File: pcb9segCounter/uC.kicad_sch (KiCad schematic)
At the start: 15 parts, among them J1 SAO, J2 AVR-ISP-6, U1 ATtiny84A-SS

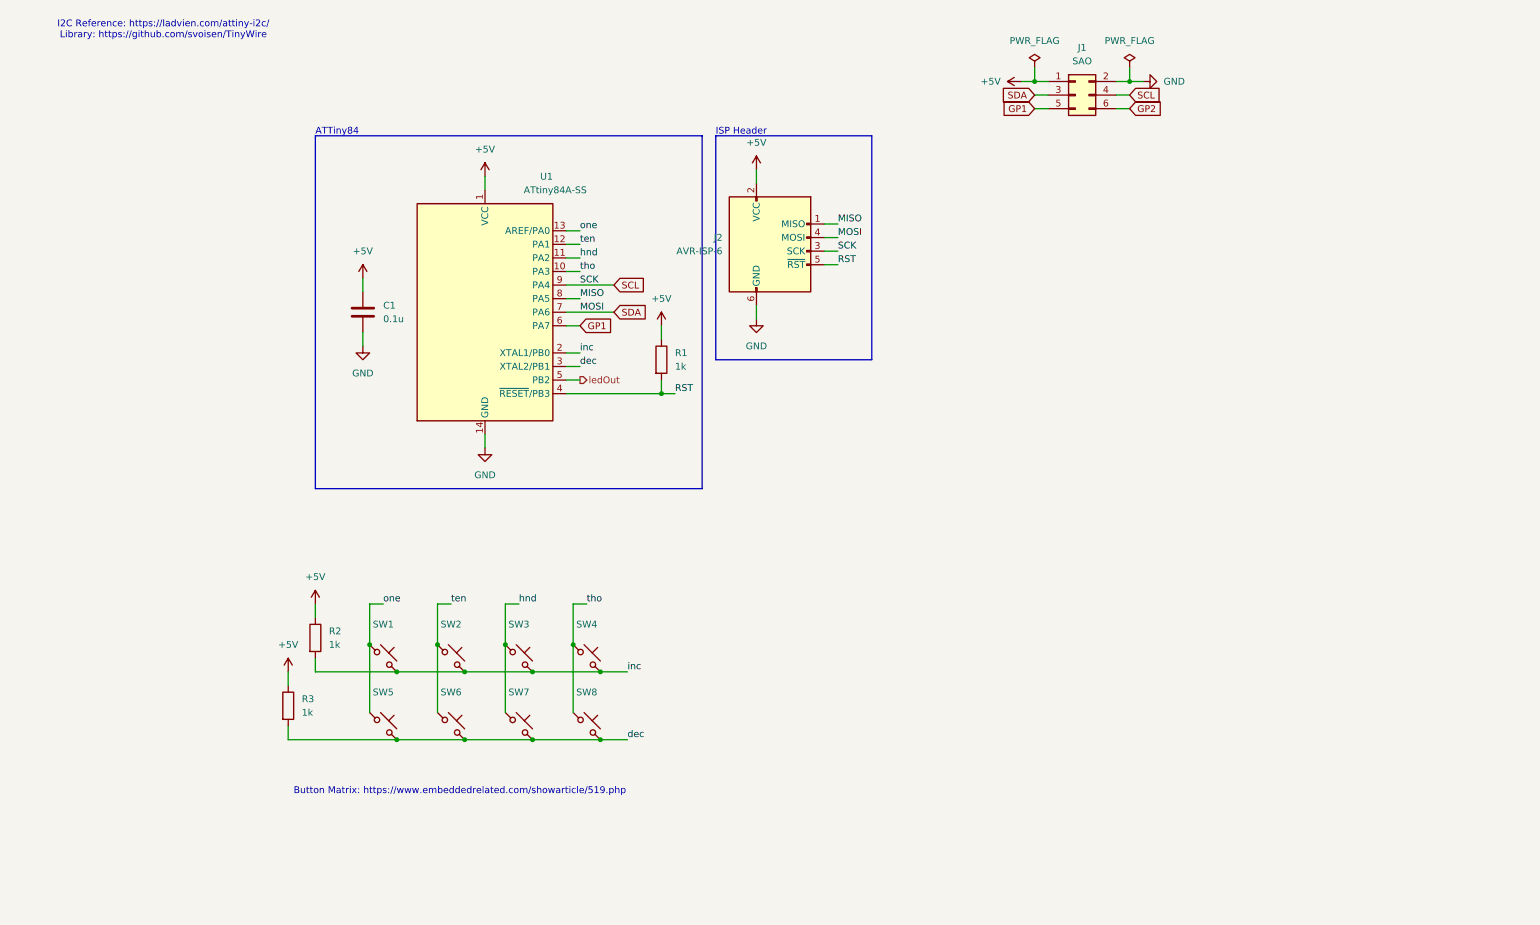
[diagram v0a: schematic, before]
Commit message: reduced to 2 digits, added capacitors
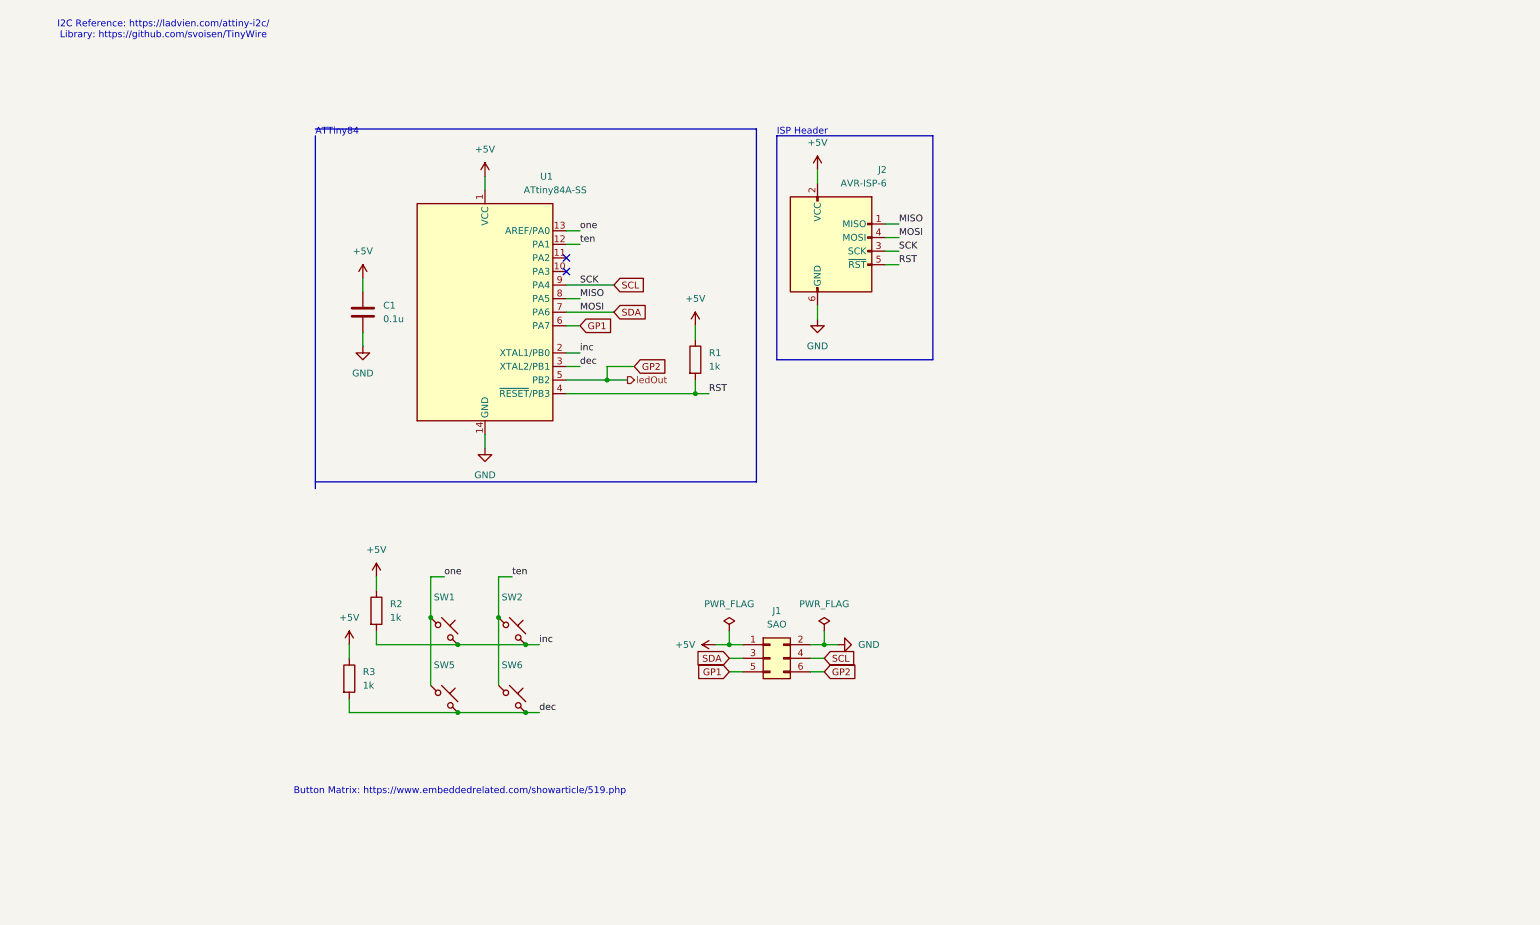
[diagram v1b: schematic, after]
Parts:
- removed SW3, SW4, SW7, SW8: ~, customParts:PTS636 SK43 LFS, symbol Switch:SW_Push_45deg
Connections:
- net ledOut is gone; now on net GP2: U1.5 (PB2)
- net hnd: no longer names the net of U1.11 (PA2)
- net tho: no longer names the net of U1.10 (PA3)
- no-connect marks 0 -> 2
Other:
- moved on the sheet: J1, J2, R1, R2, R3, SW1, SW2, SW5, SW6

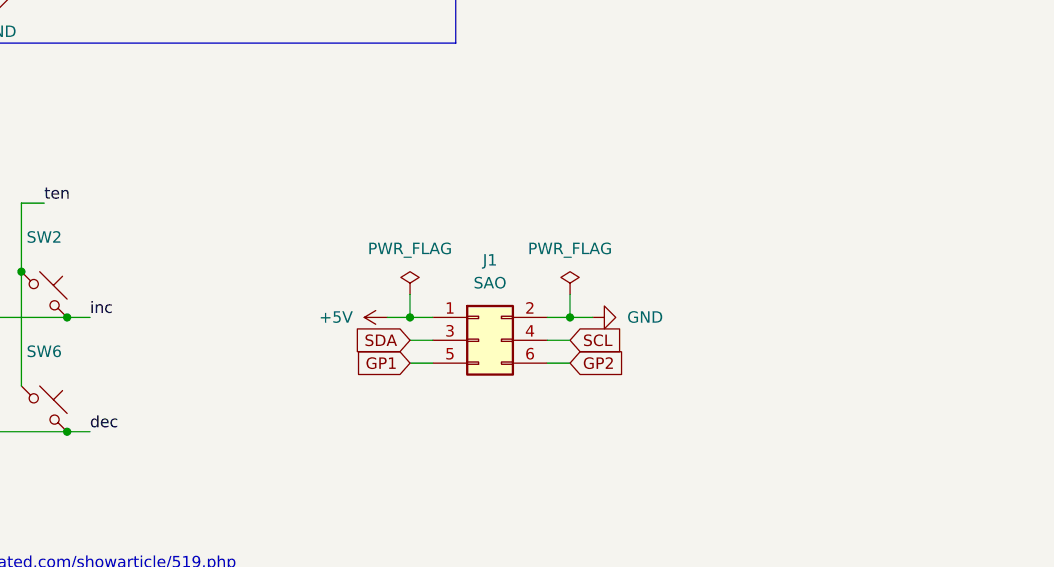
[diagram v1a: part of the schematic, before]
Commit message: adding 3d model which was used to generate board outline, commiting before adding i2c pullups
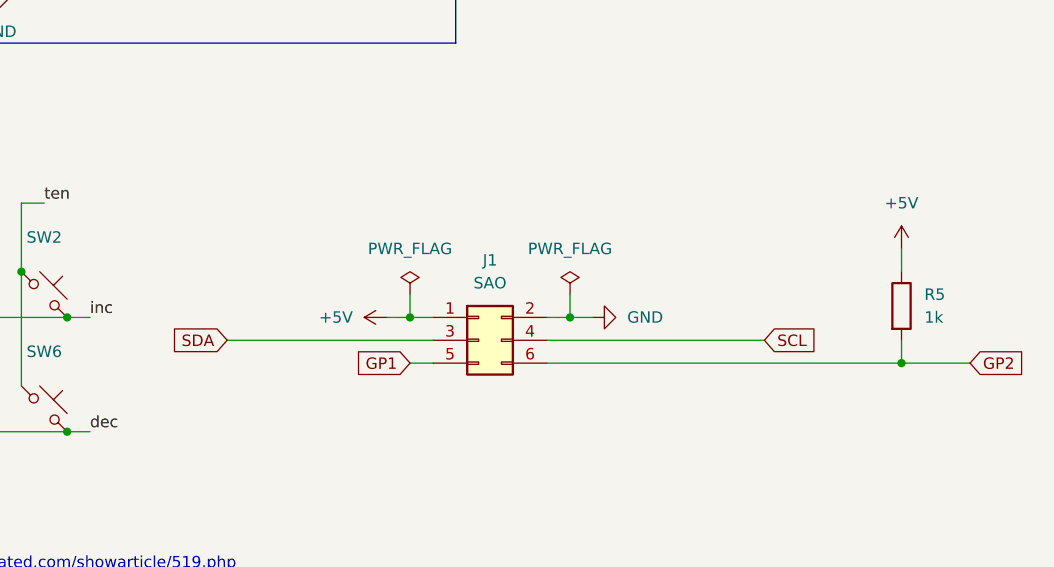
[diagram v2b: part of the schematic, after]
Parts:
- added R5: 1k, Resistor_SMD:R_0805_2012Metric, symbol Device:R
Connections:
- net +5V: now also R5.1
- net GP2: now also R5.2
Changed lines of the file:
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@@
+		(color 0 0 0 0)
+	)
+	(junction
+		(at 198.12 144.78)
+		(diameter 0)
 		(color 0 0 0 0)
 	)
@@
 		)
 	)
+	(wire
+		(pts
+			(xy 198.12 132.08) (xy 198.12 134.62)
+		)
+		(stroke
+			(width 0)
+			(type default)
+		)
+	)
 	(polyline
 		(pts
@@
 	(wire
 		(pts
+			(xy 198.12 142.24) (xy 198.12 144.78)
+		)
+		(stroke
+			(width 0)
+			(type default)
+		)
+	)
+	(wire
+		(pts
 			(xy 172.72 68.58) (xy 175.26 68.58)
 		)
@@
 	(wire
 		(pts
-			(xy 143.51 142.24) (xy 146.05 142.24)
+			(xy 123.19 142.24) (xy 146.05 142.24)
 		)
 		(stroke
@@
 	(wire
 		(pts
-			(xy 158.75 144.78) (xy 161.29 144.78)
+			(xy 158.75 144.78) (xy 198.12 144.78)
 		)
 		(stroke
@@
 	(wire
 		(pts
-			(xy 158.75 142.24) (xy 161.29 142.24)
+			(xy 158.75 142.24) (xy 182.88 142.24)
+		)
+		(stroke
+			(width 0)
+			(type default)
+		)
+	)
+	(wire
+		(pts
+			(xy 198.12 144.78) (xy 205.74 144.78)
 		)
 		(stroke
@@
 	(global_label "SCL"
 		(shape input)
-		(at 161.29 142.24 0)
+		(at 182.88 142.24 0)
 		(fields_autoplaced yes)
 		(effects
@@
 		)
 		(property "Intersheetrefs" "${INTERSHEET_REFS}"
-			(at 167.7828 142.24 0)
+			(at 189.3728 142.24 0)
 			(effects
 				(font
@@
 	(global_label "GP2"
 		(shape input)
-		(at 161.29 144.78 0)
+		(at 205.74 144.78 0)
 		(fields_autoplaced yes)
 		(effects
@@
 		)
 		(property "Intersheetrefs" "${INTERSHEET_REFS}"
-			(at 168.0247 144.78 0)
+			(at 212.4747 144.78 0)
 			(effects
 				(font
@@
 	(global_label "SDA"
 		(shape input)
-		(at 143.51 142.24 180)
+		(at 123.19 142.24 180)
 		(fields_autoplaced yes)
 		(effects
@@
 		)
 		(property "Intersheetrefs" "${INTERSHEET_REFS}"
-			(at 136.9567 142.24 0)
+			(at 116.6367 142.24 0)
 			(effects
 				(font
@@
 	)
 	(symbol
+		(lib_id "power:+5V")
+		(at 198.12 132.08 0)
+		(unit 1)
+		(exclude_from_sim no)
+		(in_bom yes)
+		(on_board yes)
+		(dnp no)
+		(fields_autoplaced yes)
+		(property "Reference" "#PWR05"
+			(at 198.12 135.89 0)
+			(effects
+				(font
+					(size 1.27 1.27)
+				)
+				(hide yes)
+			)
+		)
+		(property "Value" "+5V"
+			(at 198.12 127 0)
+			(effects
+				(font
+					(size 1.27 1.27)
+				)
+			)
+		)
+		(property "Footprint" ""
+			(at 198.12 132.08 0)
+			(effects
+				(font
+					(size 1.27 1.27)
+				)
+				(hide yes)
+			)
+		)
+		(property "Datasheet" ""
+			(at 198.12 132.08 0)
+			(effects
+				(font
+					(size 1.27 1.27)
+				)
+				(hide yes)
+			)
+		)
+		(property "Description" "Power symbol creates a global label with name \"+5V\""
+			(at 198.12 132.08 0)
+			(effects
+				(font
+					(size 1.27 1.27)
+				)
+				(hide yes)
+			)
+		)
+		(pin "1"
+		)
+		(instances
+			(project "pcb9segCounter"
+				(path "/c50b0073-6340-498a-8f0c-212ef3b3c0fe/517a53d5-7656-4587-9e33-3f758e9574ab"
+					(reference "#PWR05")
+					(unit 1)
+				)
+			)
+		)
+	)
+	(symbol
 		(lib_id "Switch:SW_Push_45deg")
 		(at 90.17 137.16 0)
@@
 					(unit 1)
 				)
+			)
+		)
+	)
+	(symbol
+		(lib_id "Device:R")
+		(at 198.12 138.43 0)
+		(unit 1)
+		(exclude_from_sim no)
+		(in_bom yes)
+		(on_board yes)
+		(dnp no)
+		(fields_autoplaced yes)
+		(property "Reference" "R5"
+			(at 200.66 137.1599 0)
+			(effects
+				(font
+					(size 1.27 1.27)
+				)
+				(justify left)
+			)
+		)
+		(property "Value" "1k"
+			(at 200.66 139.6999 0)
+			(effects
+				(font
+					(size 1.27 1.27)
+				)
+				(justify left)
+			)
+		)
+		(property "Footprint" "Resistor_SMD:R_0805_2012Metric"
+			(at 196.342 138.43 90)
+			(effects
+				(font
+					(size 1.27 1.27)
+				)
+				(hide yes)
+			)
+		)
+		(property "Datasheet" "~"
+			(at 198.12 138.43 0)
+			(effects
+				(font
+					(size 1.27 1.27)
+				)
+				(hide yes)
+			)
+		)
+		(property "Description" "Resistor"
+			(at 198.12 138.43 0)
+			(effects
+				(font
+					(size 1.27 1.27)
+				)
+				(hide yes)
+			)
+		)
+		(pin "2"
+		)
+		(pin "1"
+		)
+		(instances
+			(project ""
+				(path "/c50b0073-6340-498a-8f0c-212ef3b3c0fe/517a53d5-7656-4587-9e33-3f758e9574ab"
+					(reference "R5")
+					(unit 1)
+				)

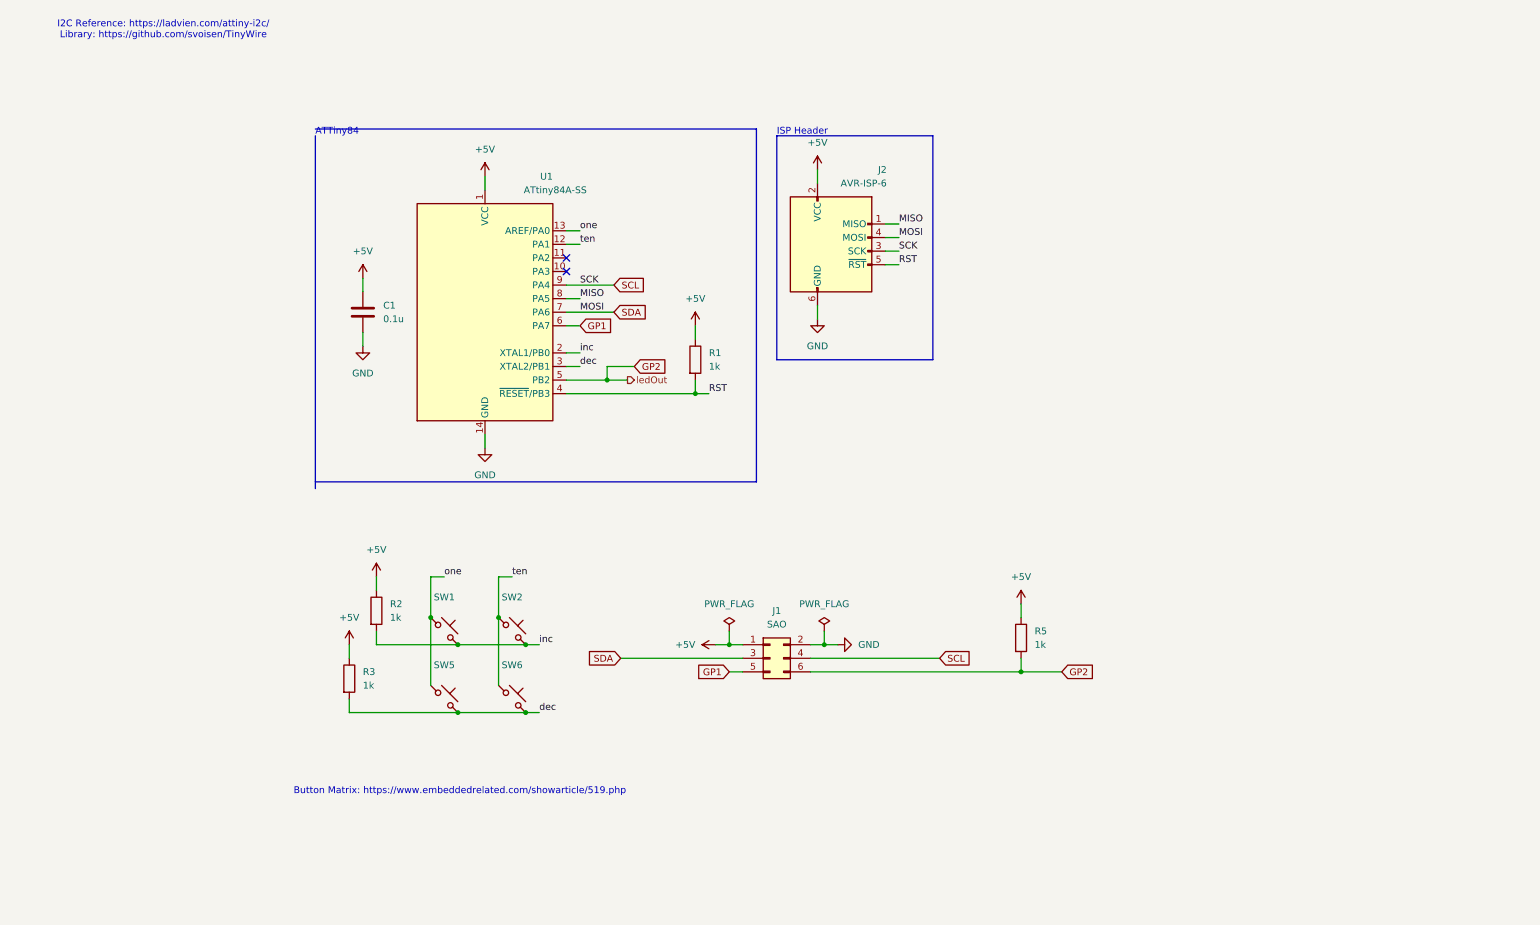
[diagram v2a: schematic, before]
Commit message: Looks really good, all footprints and implementation check out. Looking to move an LED and adding an additional decap capacitor
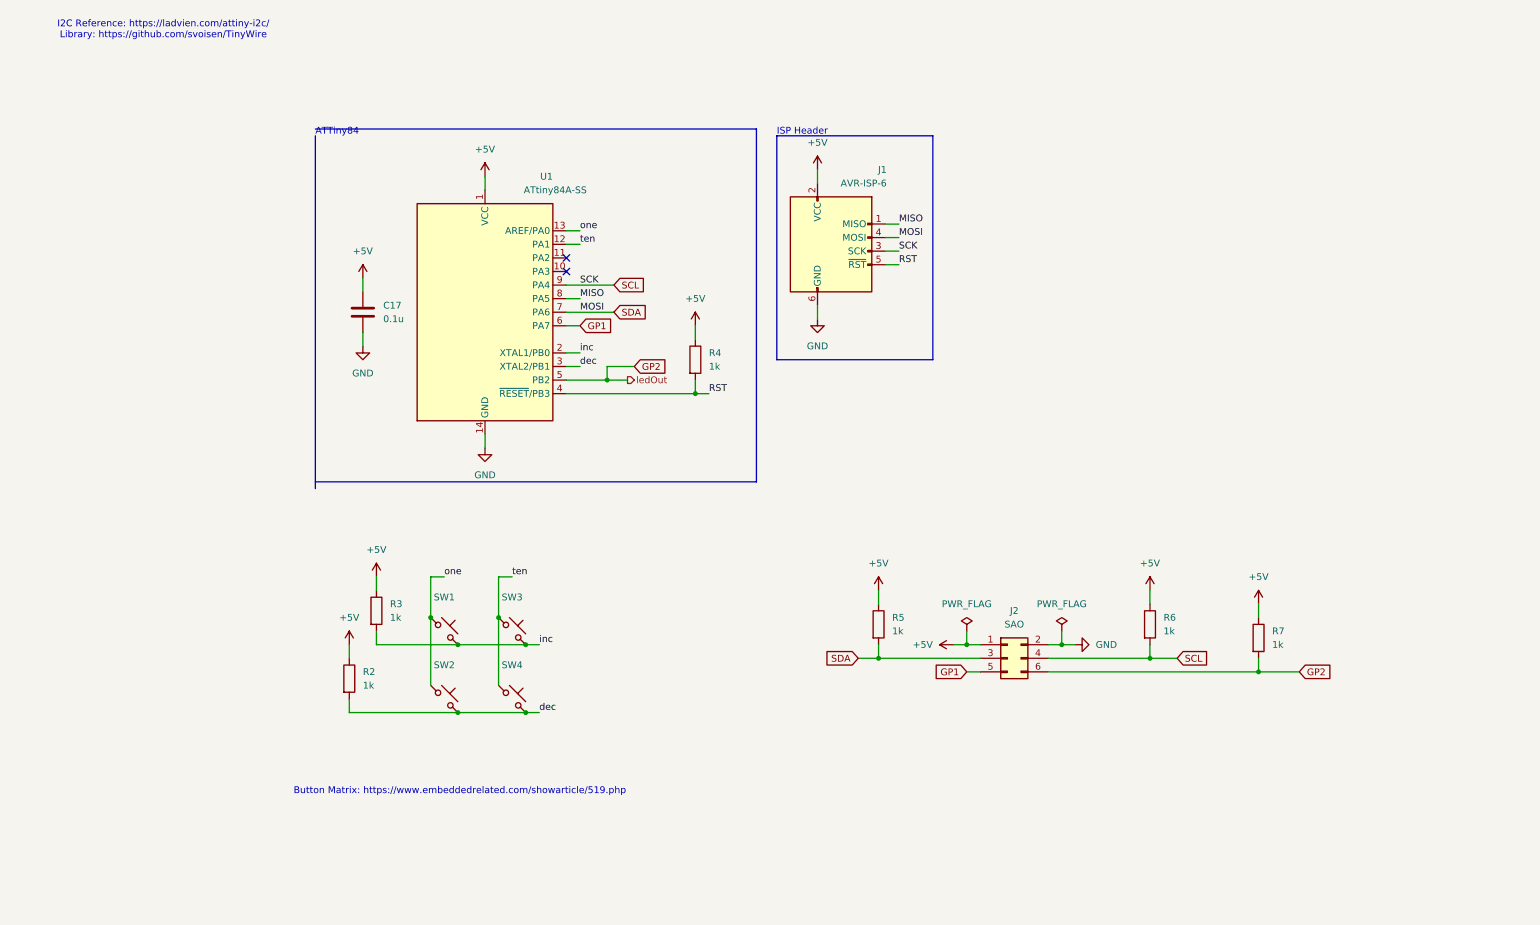
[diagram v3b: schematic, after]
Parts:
- added R5, R6: 1k, Resistor_SMD:R_0805_2012Metric, symbol Device:R
- C17: renamed from C1; footprintCheck (none) -> y
- J2: renamed from J1; footprintCheck (none) -> y; implementationCheck (none) -> y
- R2: renamed from R3; footprintCheck (none) -> y; implementationCheck (none) -> y
- R3: renamed from R2; footprintCheck (none) -> y; implementationCheck (none) -> y
- R4: renamed from R1; footprintCheck (none) -> y
- R7: renamed from R5; footprintCheck (none) -> y; implementationCheck (none) -> y
- SW1: footprintCheck (none) -> y; implementationCheck (none) -> y
- SW2: renamed from SW5; footprintCheck (none) -> y; implementationCheck (none) -> y
- SW3: renamed from SW2; footprintCheck (none) -> y; implementationCheck (none) -> y
- SW4: renamed from SW6; footprintCheck (none) -> y; implementationCheck (none) -> y
- renumbered J2 to J1
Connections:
- net +5V: now also R5.1, R6.1
- net SCL: now also R6.2
- net SDA: now also R5.2
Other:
- moved on the sheet: J2, R7

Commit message: Everything looks good for manufacture
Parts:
- renumbered C17 to C19
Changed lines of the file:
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@@
 		(dnp no)
 		(fields_autoplaced yes)
-		(property "Reference" "C17"
+		(property "Reference" "C19"
 			(at 78.74 76.1999 0)
 			(effects
@@
 			(project "pcb9segCounter"
 				(path "/c50b0073-6340-498a-8f0c-212ef3b3c0fe/517a53d5-7656-4587-9e33-3f758e9574ab"
-					(reference "C17")
+					(reference "C19")
 					(unit 1)
 				)

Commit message: Updated details to export BOM
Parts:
- J2: MFG (none) -> Amphenol FCI; MPN (none) -> 10129381-906002BLF
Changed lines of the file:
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@@
 		)
 		(instances
-			(project ""
+			(project "pcb9segCounter"
 				(path "/c50b0073-6340-498a-8f0c-212ef3b3c0fe/517a53d5-7656-4587-9e33-3f758e9574ab"
 					(reference "SW1")
@@
 			)
 		)
+		(property "MFG" "Amphenol FCI "
+			(at 195.58 142.24 0)
+			(effects
+				(font
+					(size 1.27 1.27)
+				)
+				(hide yes)
+			)
+		)
+		(property "MPN" "10129381-906002BLF"
+			(at 195.58 142.24 0)
+			(effects
+				(font
+					(size 1.27 1.27)
+				)
+				(hide yes)
+			)
+		)
 		(pin "2"
 		)
@@
 		)
 		(instances
-			(project ""
+			(project "pcb9segCounter"
 				(path "/c50b0073-6340-498a-8f0c-212ef3b3c0fe/517a53d5-7656-4587-9e33-3f758e9574ab"
 					(reference "R7")
@@
 		)
 		(instances
-			(project ""
+			(project "pcb9segCounter"
 				(path "/c50b0073-6340-498a-8f0c-212ef3b3c0fe/517a53d5-7656-4587-9e33-3f758e9574ab"
 					(reference "R3")
